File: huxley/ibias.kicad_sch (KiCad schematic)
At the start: 24 parts, among them J21 61300211121, J25 61300211121, J26 61300211121, J27 61300211121, J28 61300211121, J29 61300211121, J30 61300211121, J31 61300211121, U2 LM134H, U4 TMUX1112PWR, U5 TMUX1112PWR

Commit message: layout_1010
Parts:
- C16, C19: symbol pspice:C -> Device:C_Small
- C17, C18: value 10u -> 0.1u; symbol pspice:C -> Device:C_Small
- U2: footprint 0_726_footprints:lm134 -> Package_TO_SOT_THT:TO-46-3

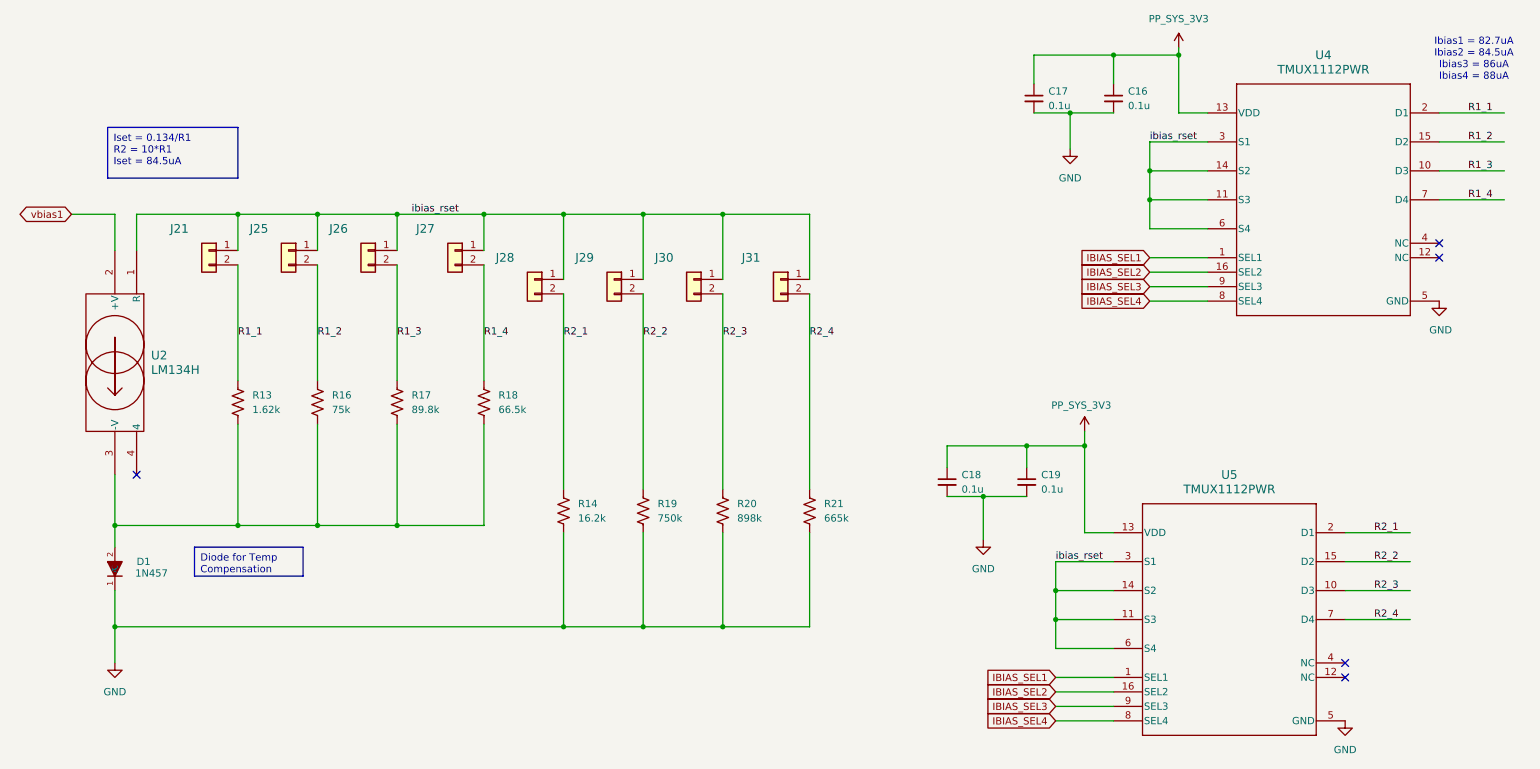
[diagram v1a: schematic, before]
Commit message: minor schematic cleanup; addition of mounting holes; minor layout adjustment
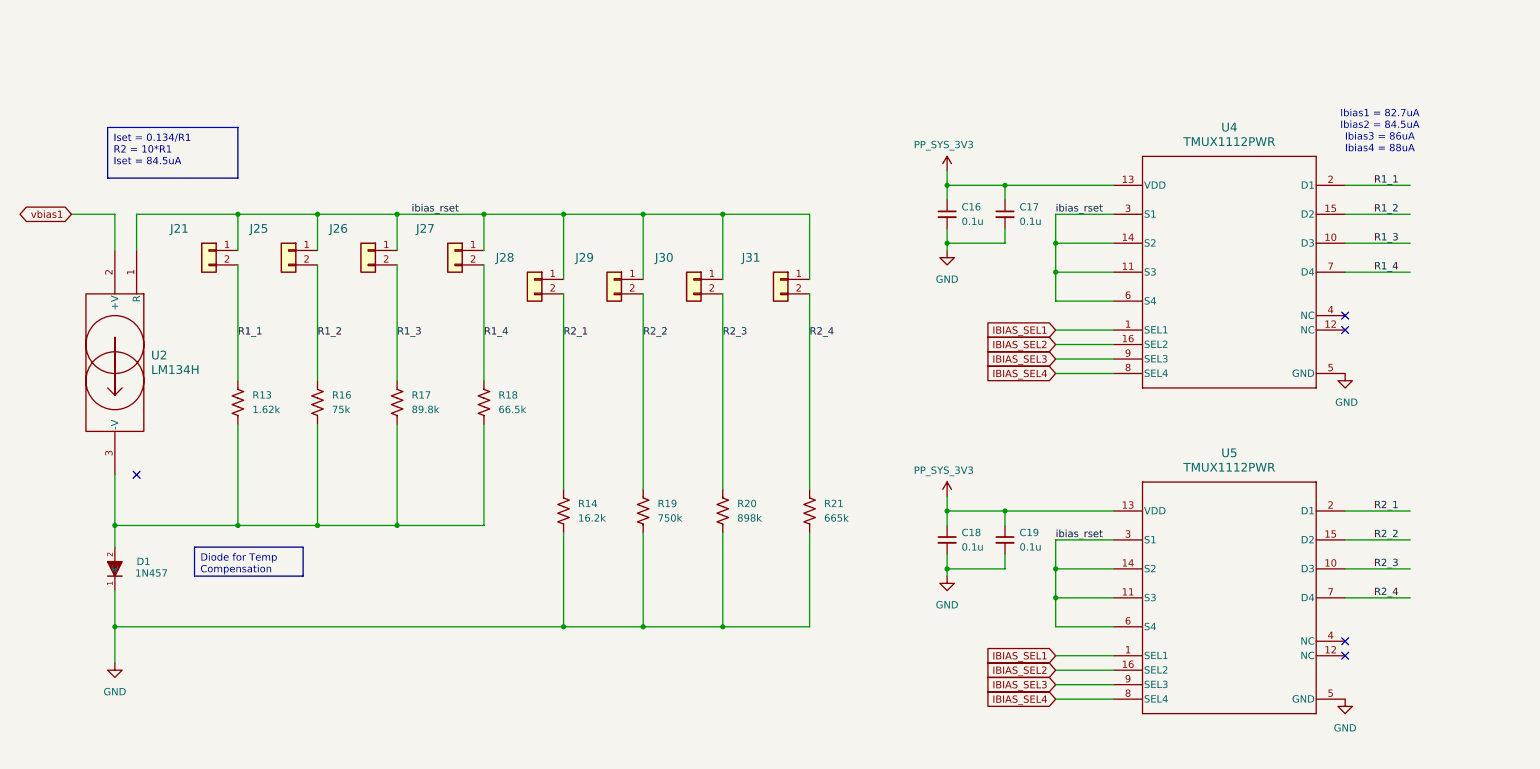
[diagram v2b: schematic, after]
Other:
- moved on the sheet: C18, C19, U4, U5

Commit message: general rerrange struct inpl
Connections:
- net IBIAS_SEL2: now also U4.8 (SEL4), U5.8 (SEL4); no longer U4.16 (SEL2), U5.16 (SEL2)
- net IBIAS_SEL4: now also U4.16 (SEL2), U5.16 (SEL2); no longer U4.8 (SEL4), U5.8 (SEL4)
- net R1_2: now also U4.7 (D4); no longer U4.15 (D2)
- net R1_4: now also U4.15 (D2); no longer U4.7 (D4)
- net R2_2: now also U5.7 (D4); no longer U5.15 (D2)
- net R2_4: now also U5.15 (D2); no longer U5.7 (D4)
- net ibias_m: now reaches D1.2 (A), R13.2, R16.2, R17.2, R18.2, U2.3 (-V)
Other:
- note added: "note swap here"
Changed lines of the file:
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@@
+		)
+	)
+	(text "note swap here"
+		(exclude_from_sim no)
+		(at 194.818 80.772 0)
+		(effects
+			(font
+				(size 1.27 1.27)
+			)
+		)
+	)
+	(text "note swap here"
+		(exclude_from_sim no)
+		(at 195.072 138.176 0)
+		(effects
+			(font
+				(size 1.27 1.27)
+			)
 		)
 	)
@@
 		)
 	)
-	(label "R2_2"
+	(label "R2_4"
 		(at 256.54 106.68 0)
 		(fields_autoplaced yes)
@@
 		)
 	)
-	(label "R2_4"
+	(label "R2_2"
 		(at 256.54 116.84 0)
+		(fields_autoplaced yes)
+		(effects
+			(font
+				(size 1.27 1.27)
+			)
+			(justify left bottom)
+		)
+	)
+	(label "ibias_m"
+		(at 45.72 104.14 0)
 		(fields_autoplaced yes)
 		(effects
@@
 		)
 	)
+	(label "R1_2"
+		(at 256.54 59.69 0)
+		(fields_autoplaced yes)
+		(effects
+			(font
+				(size 1.27 1.27)
+			)
+			(justify left bottom)
+		)
+	)
 	(label "R1_4"
-		(at 256.54 59.69 0)
-		(fields_autoplaced yes)
-		(effects
-			(font
-				(size 1.27 1.27)
-			)
-			(justify left bottom)
-		)
-	)
-	(label "R1_2"
 		(at 256.54 49.53 0)
 		(fields_autoplaced yes)
@@
 		)
 	)
+	(global_label "IBIAS_SEL2"
+		(shape input)
+		(at 200.66 134.62 180)
+		(fields_autoplaced yes)
+		(effects
+			(font
+				(size 1.27 1.27)
+			)
+			(justify right)
+		)
+		(property "Intersheetrefs" "${INTERSHEET_REFS}"
+			(at 187.3334 134.62 0)
+			(effects
+				(font
+					(size 1.27 1.27)
+				)
+				(justify right)
+				(hide yes)
+			)
+		)
+	)
+	(global_label "IBIAS_SEL1"
+		(shape input)
+		(at 200.66 69.85 180)
+		(fields_autoplaced yes)
+		(effects
+			(font
+				(size 1.27 1.27)
+			)
+			(justify right)
+		)
+		(property "Intersheetrefs" "${INTERSHEET_REFS}"
+			(at 187.3334 69.85 0)
+			(effects
+				(font
+					(size 1.27 1.27)
+				)
+				(justify right)
+				(hide yes)
+			)
+		)
+	)
+	(global_label "IBIAS_SEL2"
+		(shape input)
+		(at 200.66 77.47 180)
+		(fields_autoplaced yes)
+		(effects
+			(font
+				(size 1.27 1.27)
+			)
+			(justify right)
+		)
+		(property "Intersheetrefs" "${INTERSHEET_REFS}"
+			(at 187.3334 77.47 0)
+			(effects
+				(font
+					(size 1.27 1.27)
+				)
+				(justify right)
+				(hide yes)
+			)
+		)
+	)
+	(global_label "IBIAS_SEL3"
+		(shape input)
+		(at 200.66 132.08 180)
+		(fields_autoplaced yes)
+		(effects
+			(font
+				(size 1.27 1.27)
+			)
+			(justify right)
+		)
+		(property "Intersheetrefs" "${INTERSHEET_REFS}"
+			(at 187.3334 132.08 0)
+			(effects
+				(font
+					(size 1.27 1.27)
+				)
+				(justify right)
+				(hide yes)
+			)
+		)
+	)
 	(global_label "IBIAS_SEL4"
-		(shape input)
-		(at 200.66 134.62 180)
-		(fields_autoplaced yes)
-		(effects
-			(font
-				(size 1.27 1.27)
-			)
-			(justify right)
-		)
-		(property "Intersheetrefs" "${INTERSHEET_REFS}"
-			(at 187.3334 134.62 0)
-			(effects
-				(font
-					(size 1.27 1.27)
-				)
-				(justify right)
-				(hide yes)
-			)
-		)
-	)
-	(global_label "IBIAS_SEL1"
-		(shape input)
-		(at 200.66 69.85 180)
-		(fields_autoplaced yes)
-		(effects
-			(font
-				(size 1.27 1.27)
-			)
-			(justify right)
-		)
-		(property "Intersheetrefs" "${INTERSHEET_REFS}"
-			(at 187.3334 69.85 0)
-			(effects
-				(font
-					(size 1.27 1.27)
-				)
-				(justify right)
-				(hide yes)
-			)
-		)
-	)
-	(global_label "IBIAS_SEL4"
-		(shape input)
-		(at 200.66 77.47 180)
-		(fields_autoplaced yes)
-		(effects
-			(font
-				(size 1.27 1.27)
-			)
-			(justify right)
-		)
-		(property "Intersheetrefs" "${INTERSHEET_REFS}"
-			(at 187.3334 77.47 0)
-			(effects
-				(font
-					(size 1.27 1.27)
-				)
-				(justify right)
-				(hide yes)
-			)
-		)
-	)
-	(global_label "IBIAS_SEL3"
-		(shape input)
-		(at 200.66 132.08 180)
-		(fields_autoplaced yes)
-		(effects
-			(font
-				(size 1.27 1.27)
-			)
-			(justify right)
-		)
-		(property "Intersheetrefs" "${INTERSHEET_REFS}"
-			(at 187.3334 132.08 0)
-			(effects
-				(font
-					(size 1.27 1.27)
-				)
-				(justify right)
-				(hide yes)
-			)
-		)
-	)
-	(global_label "IBIAS_SEL2"
 		(shape input)
 		(at 200.66 129.54 180)
@@
 		)
 	)
-	(global_label "IBIAS_SEL2"
+	(global_label "IBIAS_SEL4"
 		(shape input)
 		(at 200.66 72.39 180)
